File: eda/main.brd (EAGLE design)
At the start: 55.9 x 53.3 mm, 10 parts, among them U1 SC0915

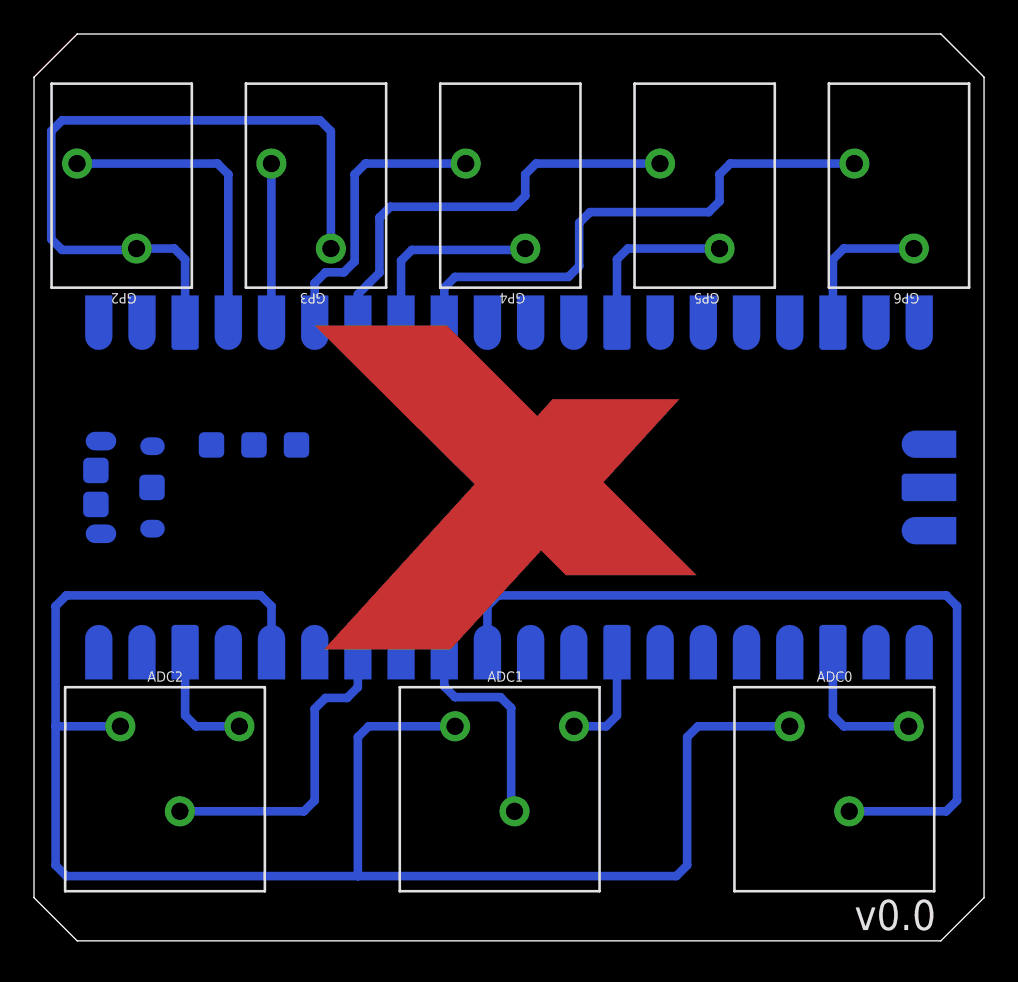
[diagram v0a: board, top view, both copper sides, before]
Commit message: Modified board to reflect fixed 3 pos footprint.
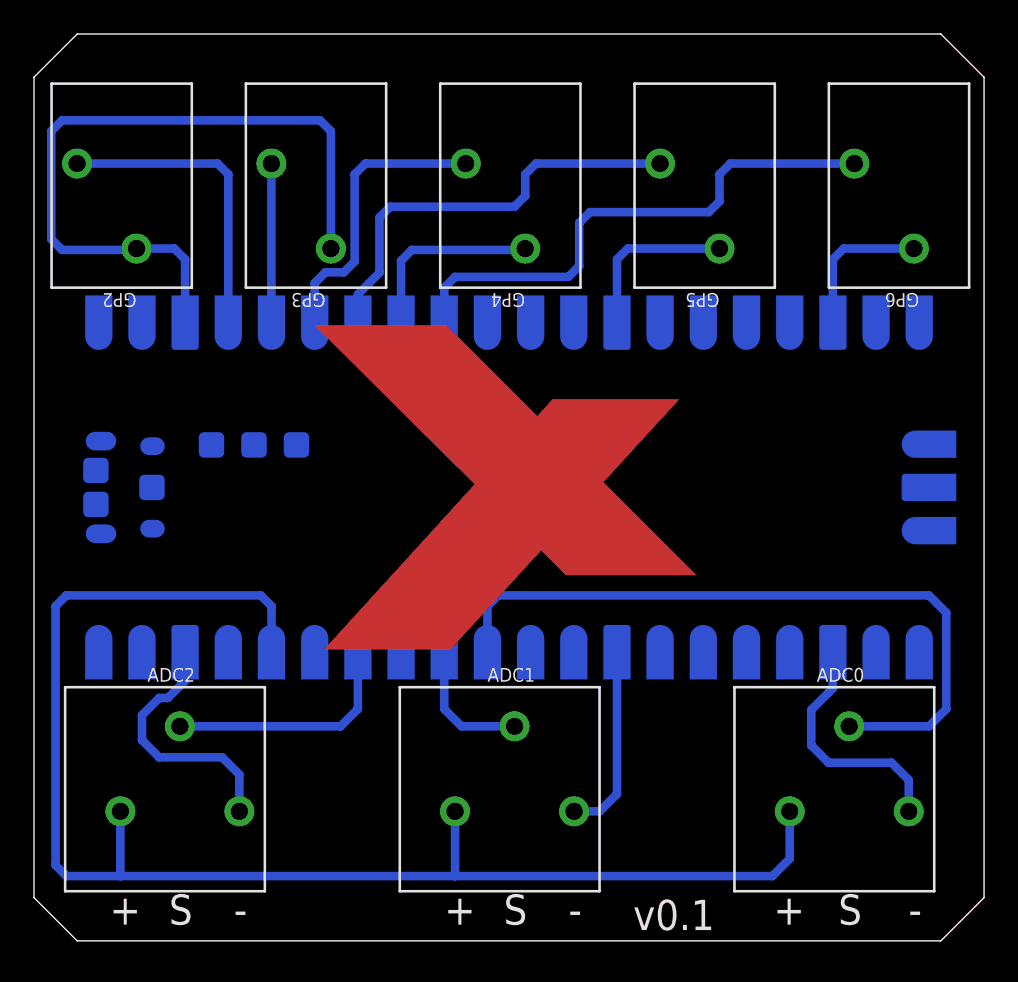
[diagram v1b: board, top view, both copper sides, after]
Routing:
- net GND: track 96.5 -> 115.8 mm
- net +3.3V: track 100.6 -> 85.4 mm
- net ADC0: track 48.9 -> 42.2 mm
- net ADC1: track 12.8 -> 7.90 mm
- net ADC2: track 18.7 -> 14.2 mm
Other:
- board text added: "+"
- board text added: "-"
- board text added: "S"
- board text added: "v0.1"
- board text removed: "v0.0"
